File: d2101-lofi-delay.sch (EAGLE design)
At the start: 84 parts, among them U1 FX2-20P-1.27DS, U2 FX2-20S-1.27DS

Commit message: d2101 controls placement fix
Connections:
- net FBK_INT_LEFT: now also SA2.1.2; no longer SA2.1.1
- net FBK_INT_RIGHT: now also SA2.2.2; no longer SA2.2.1
- net FBK_LEFT: now also SA2.1.1; no longer SA2.1.2
- net FBK_RIGHT: now also SA2.2.1; no longer SA2.2.2
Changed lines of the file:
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@@
 <?xml version="1.0" encoding="utf-8"?>
 <!DOCTYPE eagle SYSTEM "eagle.dtd">
-<eagle version="7.5.0">
+<eagle version="7.4.1">
 <drawing>
 <settings>
@@
 </segment>
 <segment>
-<label x="205.74" y="-116.84" size="1.4224" layer="95" rot="R180" xref="yes"/>
-<pinref part="SA2" gate=".2" pin="2"/>
-<wire x1="208.28" y1="-116.84" x2="205.74" y2="-116.84" width="0.1524" layer="91"/>
+<label x="205.74" y="-114.3" size="1.4224" layer="95" rot="R180" xref="yes"/>
+<pinref part="SA2" gate=".2" pin="1"/>
+<wire x1="208.28" y1="-114.3" x2="205.74" y2="-114.3" width="0.1524" layer="91"/>
 </segment>
 </net>
@@
 </segment>
 <segment>
-<label x="205.74" y="10.16" size="1.4224" layer="95" rot="R180" xref="yes"/>
-<pinref part="SA2" gate=".1" pin="2"/>
-<wire x1="208.28" y1="10.16" x2="205.74" y2="10.16" width="0.1524" layer="91"/>
+<label x="205.74" y="12.7" size="1.4224" layer="95" rot="R180" xref="yes"/>
+<pinref part="SA2" gate=".1" pin="1"/>
+<wire x1="208.28" y1="12.7" x2="205.74" y2="12.7" width="0.1524" layer="91"/>
 </segment>
 </net>
@@
 </segment>
 <segment>
-<label x="205.74" y="12.7" size="1.4224" layer="95" rot="R180" xref="yes"/>
-<pinref part="SA2" gate=".1" pin="1"/>
-<wire x1="208.28" y1="12.7" x2="205.74" y2="12.7" width="0.1524" layer="91"/>
+<label x="205.74" y="10.16" size="1.4224" layer="95" rot="R180" xref="yes"/>
+<pinref part="SA2" gate=".1" pin="2"/>
+<wire x1="208.28" y1="10.16" x2="205.74" y2="10.16" width="0.1524" layer="91"/>
 </segment>
 </net>
@@
 </segment>
 <segment>
-<label x="205.74" y="-114.3" size="1.4224" layer="95" rot="R180" xref="yes"/>
-<pinref part="SA2" gate=".2" pin="1"/>
-<wire x1="208.28" y1="-114.3" x2="205.74" y2="-114.3" width="0.1524" layer="91"/>
-</segment>
-</net>
+<label x="205.74" y="-116.84" size="1.4224" layer="95" rot="R180" xref="yes"/>
+<pinref part="SA2" gate=".2" pin="2"/>
+<wire x1="208.28" y1="-116.84" x2="205.74" y2="-116.84" width="0.1524" layer="91"/>
+</segment>
+</net>

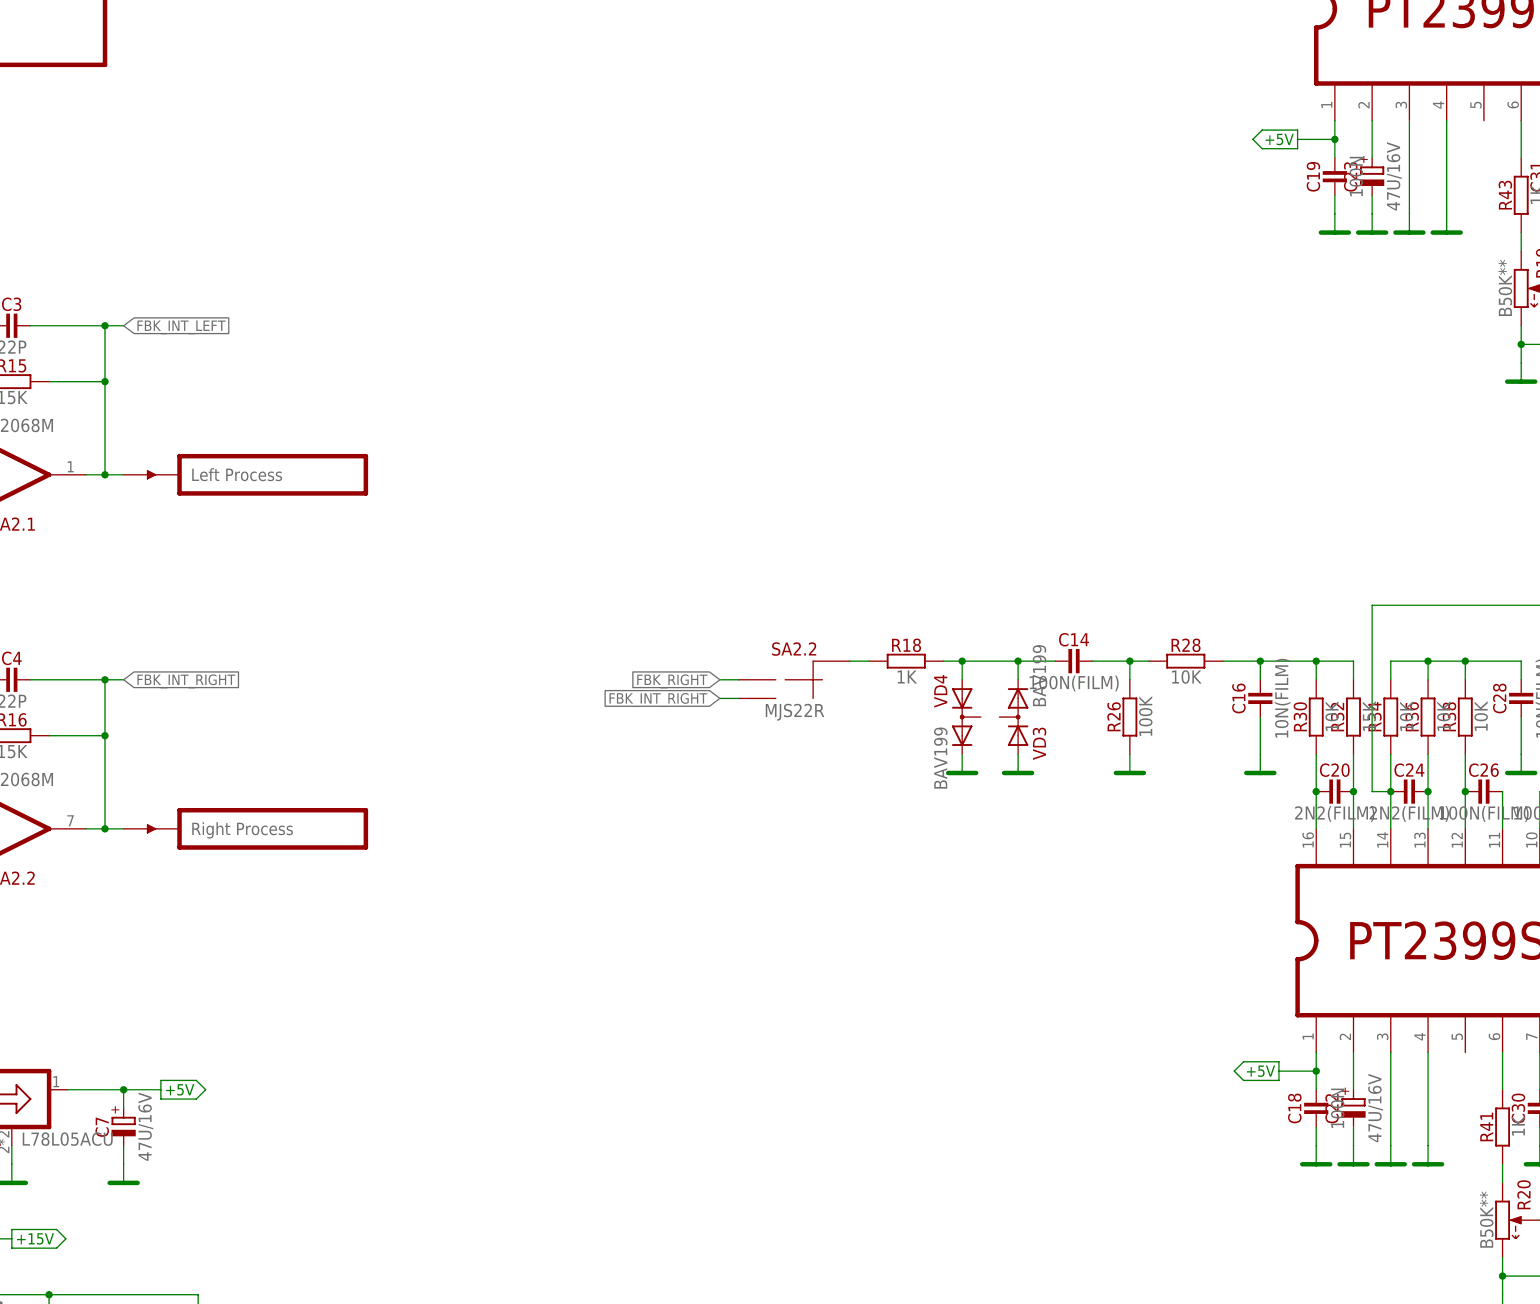
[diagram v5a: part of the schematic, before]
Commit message: Changed 47u/16V -> 10u/35V
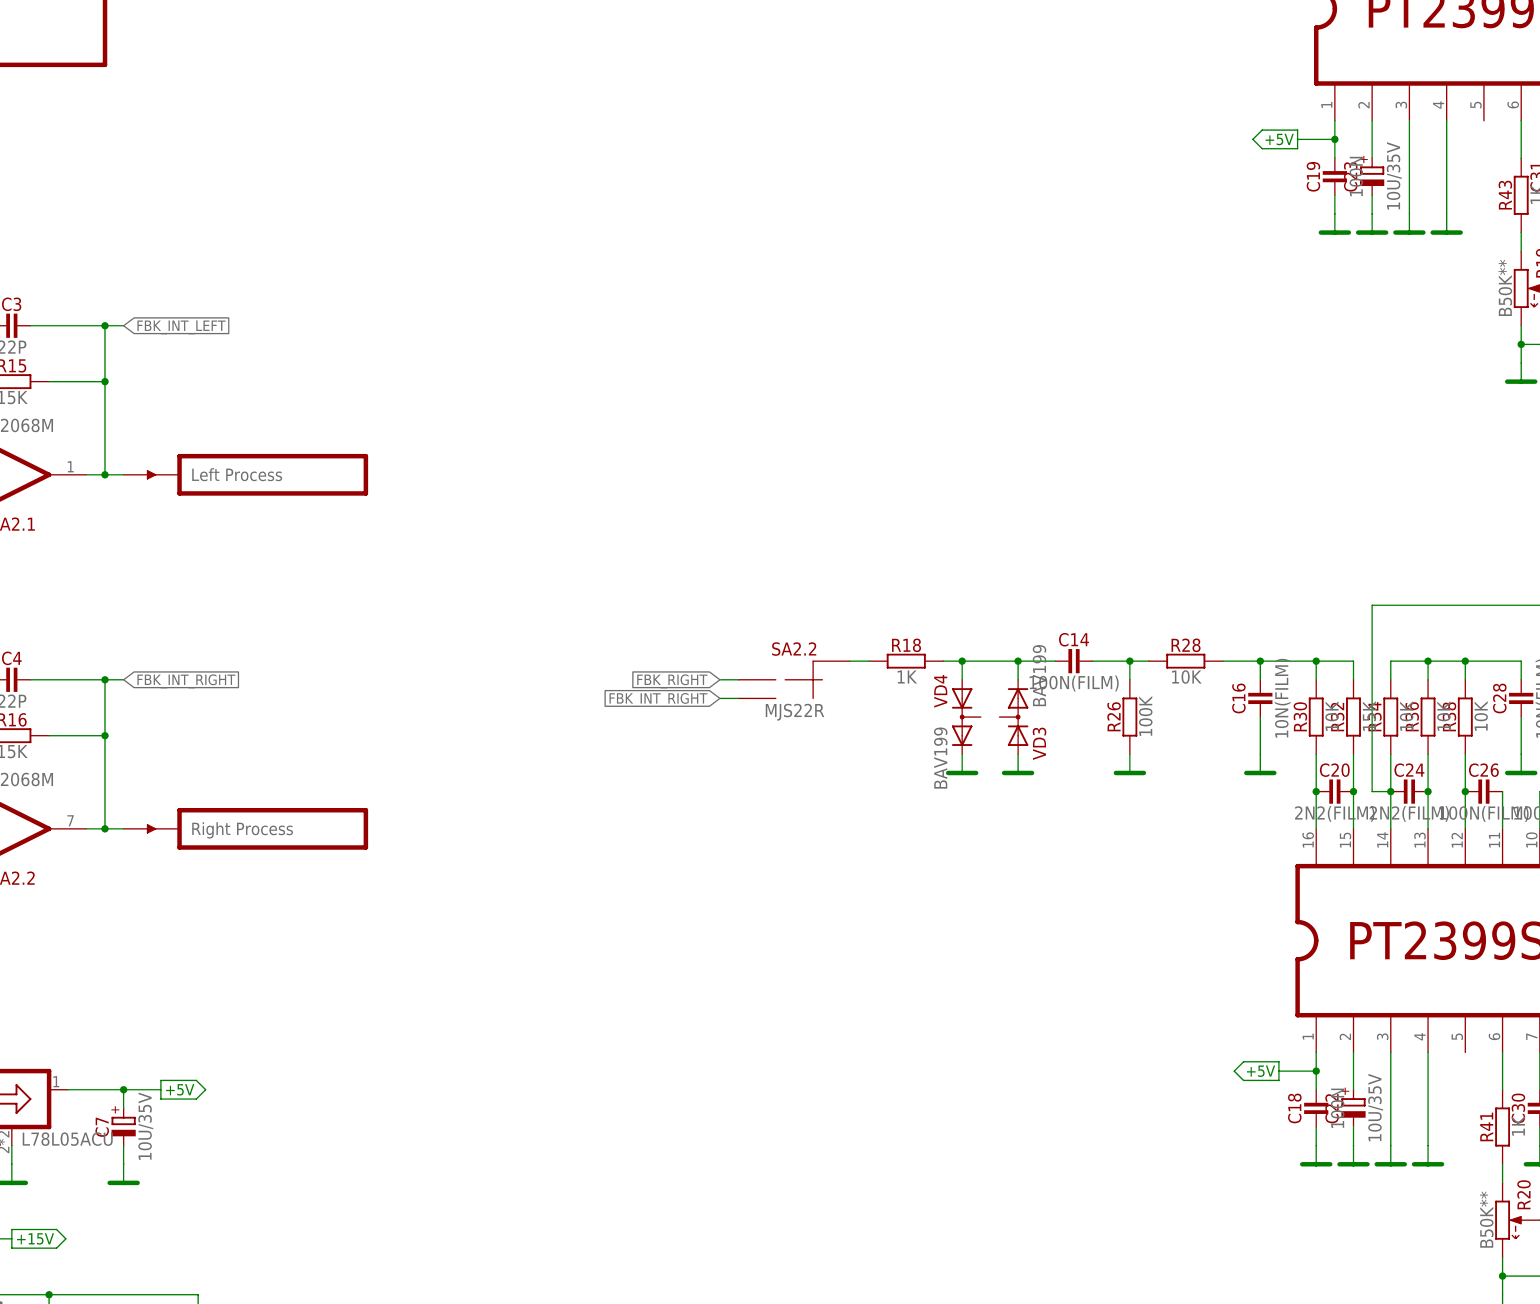
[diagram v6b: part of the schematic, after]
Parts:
- C22, C23, C7: value 47U/16V -> 10U/35V; device capacitors-electrolytic:47U/16V -> capacitors-electrolytic:10U/35V
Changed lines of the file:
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@@
 <part name="C5" library="capacitors" deviceset="?" device="100N"/>
 <part name="C6" library="capacitors" deviceset="?" device="100N"/>
-<part name="C7" library="capacitors-electrolytic" deviceset="?" device="47U/16V"/>
+<part name="C7" library="capacitors-electrolytic" deviceset="?" device="10U/35V" value="10U/35V"/>
 <part name="R29" library="resistors" deviceset="?" device="10K"/>
 <part name="C15" library="capacitors" deviceset="?" device="100N(FILM)"/>
@@
 <part name="C25" library="capacitors" deviceset="?" device="2N2(FILM)"/>
 <part name="C19" library="capacitors" deviceset="?" device="100N"/>
-<part name="C23" library="capacitors-electrolytic" deviceset="?" device="47U/16V"/>
+<part name="C23" library="capacitors-electrolytic" deviceset="?" device="10U/35V" value="10U/35V"/>
 <part name="R43" library="resistors" deviceset="?" device="1K"/>
 <part name="C31" library="capacitors" deviceset="?" device="100N"/>
@@
 <part name="C24" library="capacitors" deviceset="?" device="2N2(FILM)"/>
 <part name="C18" library="capacitors" deviceset="?" device="100N"/>
-<part name="C22" library="capacitors-electrolytic" deviceset="?" device="47U/16V"/>
+<part name="C22" library="capacitors-electrolytic" deviceset="?" device="10U/35V" value="10U/35V"/>
 <part name="R41" library="resistors" deviceset="?" device="1K"/>
 <part name="C30" library="capacitors" deviceset="?" device="100N"/>
